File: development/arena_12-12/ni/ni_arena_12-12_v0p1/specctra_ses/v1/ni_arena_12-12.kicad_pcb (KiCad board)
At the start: 6 copper layers, 228.6 x 228.6 mm, 581 parts, among them J1 Barrel_Jack, J2 NI_TE_68pos, J3 Barrel_Jack, P1 CONN15, P10 CONN15, P11 CONN15, P12 CONN15, P2 CONN15, P3 CONN15, P4 CONN15, P5 CONN15, P6 CONN15, P7 CONN15, P8 CONN15, P9 CONN15, Q1 MOSFET_NCHAN, SW1 SW_SPDT, U1 AP2112K-3.3, U10 TXB0108PW, U100 74LVC2G17, U101 74LVC2G17, U102 74LVC2G17, U103 74LVC2G17, U104 74LVC2G17, U105 74LVC2G17, U106 74LVC2G17, U107 74LVC2G17, U108 74LVC2G17, U109 74LVC2G17, U11 TXB0108PW, U110 74LVC2G17, U12 TXB0108PW, U13 TXB0108PW, U14 TXB0108PW, U15 TXB0108PW, U16 TXB0108PW, U17 TXB0108PW, U18 TXB0108PW, U19 74LVC2G17, U2 TXB0108PW, U20 74LVC2G17, U21 74LVC2G17, U22 74LVC2G17, U23 74LVC2G17, U24 74LVC2G17, U25 74LVC2G17, U26 74LVC2G17, U27 74LVC2G17, U28 74LVC2G17, U29 74LVC2G17, U3 TXB0108PW, U30 74LVC2G17, U31 74LVC2G17, U32 74LVC2G17, U33 74LVC2G17, U34 74LVC2G17, U35 74LVC2G17, U36 74LVC2G17, U37 74LVC2G17, U38 74LVC2G17, U39 74LVC2G17, U4 TXB0108PW, U40 74LVC2G17, U41 74LVC2G17, U42 74LVC2G17, U43 74LVC2G17, U44 74LVC2G17, U45 74LVC2G17, U46 74LVC2G17, U47 74LVC2G17, U48 74LVC2G17, U49 74LVC2G17, U5 TXB0108PW, U50 74LVC2G17, U51 74LVC2G17, U52 74LVC2G17, U53 74LVC2G17, U54 74LVC2G17, U55 74LVC2G17, U56 74LVC2G17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

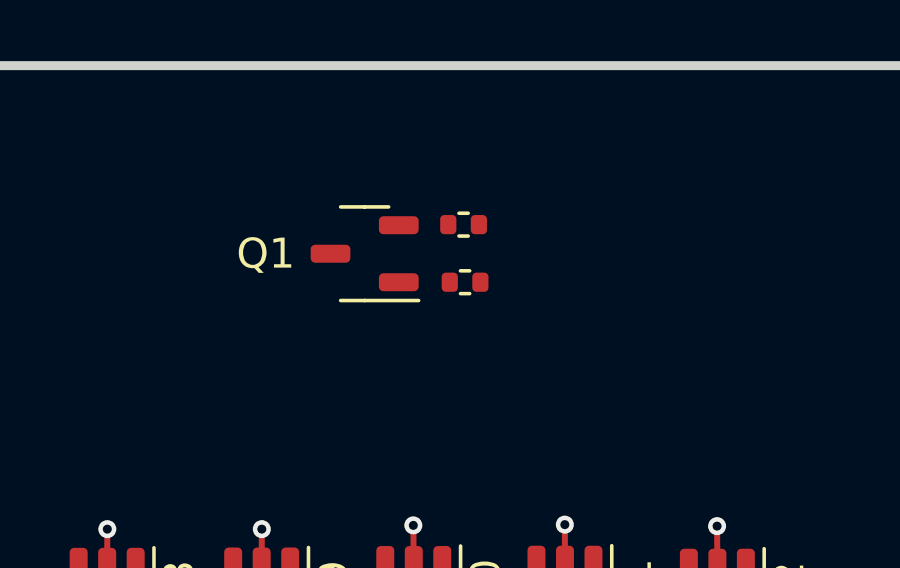
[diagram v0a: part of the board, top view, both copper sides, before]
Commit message: Complete preliminary routing of ni 12-12 arena with schmitt buffers.
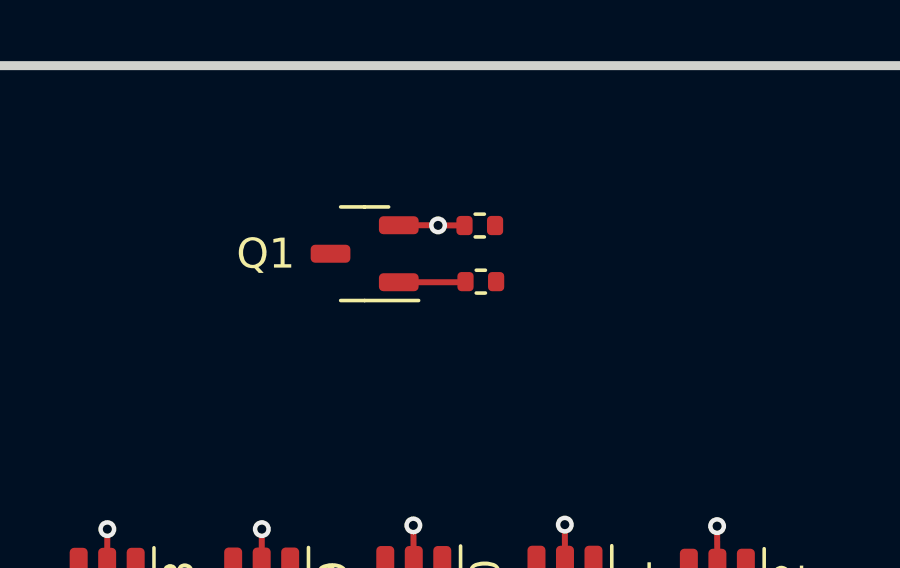
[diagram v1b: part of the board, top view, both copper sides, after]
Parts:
- moved R307 0.54 mm to (188.8, 68.8)
- moved R308 0.53 mm to (188.8, 70.7)
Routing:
- net Net-(Q1-G): track 0.00 -> 2.23 mm
- net GND: track 297.2 -> 299.4 mm, vias 259 -> 260
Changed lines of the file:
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@@
 		(1 "In1.Cu" power)
 		(2 "In2.Cu" power)
-		(3 "In3.Cu" signal)
-		(4 "In4.Cu" signal)
+		(3 "In3.Cu" power)
+		(4 "In4.Cu" power)
 		(31 "B.Cu" signal)
 		(32 "B.Adhes" user "B.Adhesive")
@@
 	(footprint "Resistor_SMD:R_0402_1005Metric"
 		(layer "F.Cu")
-		(at 188.25 68.8)
+		(at 188.79 68.83)
 		(descr "Resistor SMD 0402 (1005 Metric), square (rectangular) end terminal, IPC_7351 nominal, (Body size source: IPC-SM-782 page 72, https://www.pcb-3d.com/wordpress/wp-content/uploads/ipc-sm-782a_amendment_1_and_2.pdf), generated with kicad-footprint-generator")
 		(tags "resistor")
@@
 	(footprint "Resistor_SMD:R_0402_1005Metric"
 		(layer "F.Cu")
-		(at 188.3 70.72)
+		(at 188.825 70.7)
 		(descr "Resistor SMD 0402 (1005 Metric), square (rectangular) end terminal, IPC_7351 nominal, (Body size source: IPC-SM-782 page 72, https://www.pcb-3d.com/wordpress/wp-content/uploads/ipc-sm-782a_amendment_1_and_2.pdf), generated with kicad-footprint-generator")
 		(tags "resistor")
@@
 	)
 	(segment
+		(start 188.275 68.825)
+		(end 188.28 68.83)
+		(width 0.2)
+		(layer "F.Cu")
+		(net 3)
+	)
+	(segment
 		(start 270.590028 176.38)
 		(end 269.62 176.38)
@@
 	)
 	(segment
+		(start 187.395 68.82)
+		(end 187.4 68.825)
+		(width 0.2)
+		(layer "F.Cu")
+		(net 3)
+	)
+	(segment
 		(start 80.164971 163.97)
 		(end 78.85 163.975)
@@
 	)
 	(segment
+		(start 187.4 68.825)
+		(end 188.275 68.825)
+		(width 0.2)
+		(layer "F.Cu")
+		(net 3)
+	)
+	(segment
 		(start 282.2425 131.315)
 		(end 282.2425 130.3825)
@@
 	)
 	(segment
+		(start 186.09 68.82)
+		(end 187.395 68.82)
+		(width 0.2)
+		(layer "F.Cu")
+		(net 3)
+	)
+	(segment
 		(start 260.245 108.52)
 		(end 260.25 108.525)
@@
 	)
 	(via
+		(at 187.4 68.825)
+		(size 0.6)
+		(drill 0.3)
+		(layers "F.Cu" "B.Cu")
+		(net 3)
+	)
+	(via
 		(at 78.975 158.9)
 		(size 0.6)
@@
 	)
 	(segment
+		(start 188.295 70.72)
+		(end 188.315 70.7)
+		(width 0.2)
+		(layer "F.Cu")
+		(net 202)
+	)
+	(segment
+		(start 186.09 70.72)
+		(end 188.295 70.72)
+		(width 0.2)
+		(layer "F.Cu")
+		(net 202)
+	)
+	(segment
